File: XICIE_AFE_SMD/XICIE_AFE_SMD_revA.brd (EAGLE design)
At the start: 43.2 x 34 mm, 39 parts, among them IC1 LM324D, IC2 CY8C4245T, IC3 AAT1217, J1 22-27-2021-02, Q1 MOSFET-NCHANNELBSS123LT1G, Q2 MOSFET-NCHANNELBSS123LT1G, Q3 MOSFET-NCHANNELBSS123LT1G

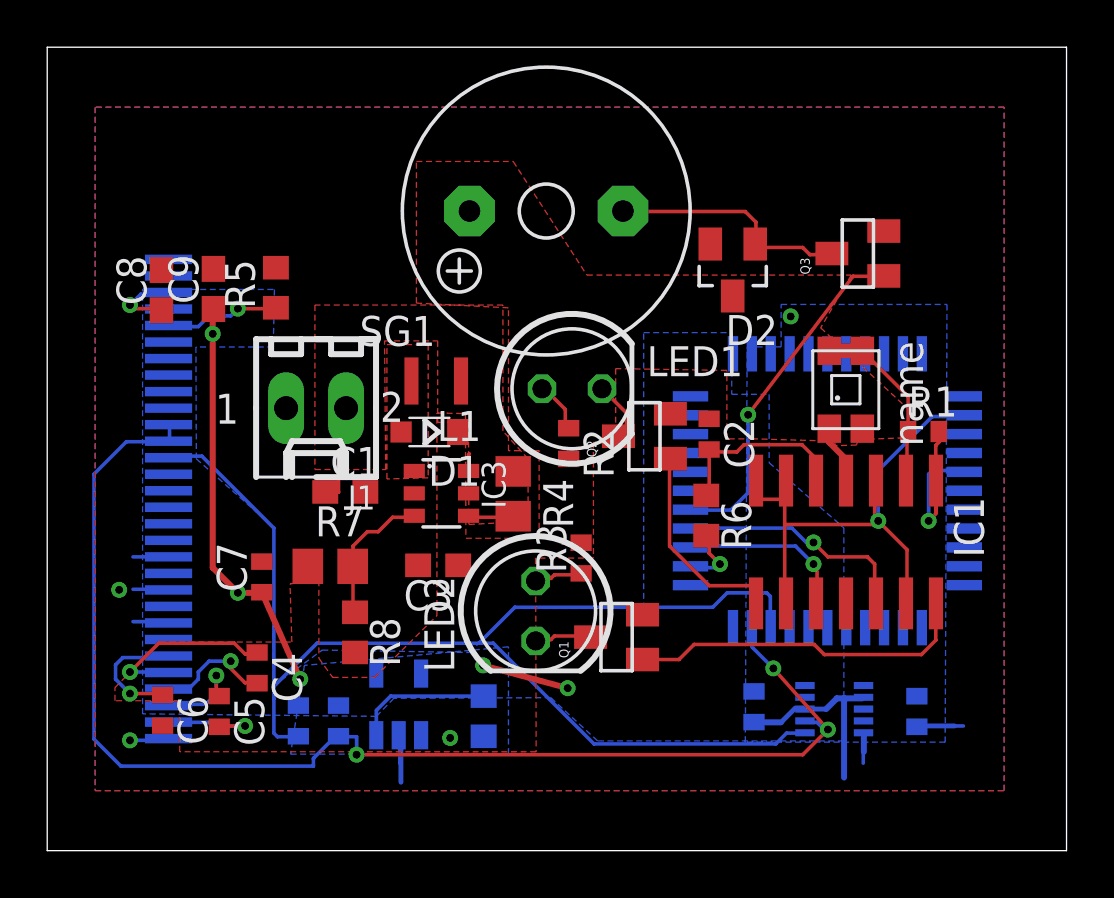
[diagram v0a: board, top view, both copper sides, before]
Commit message: Increased clearance for better manufacturing
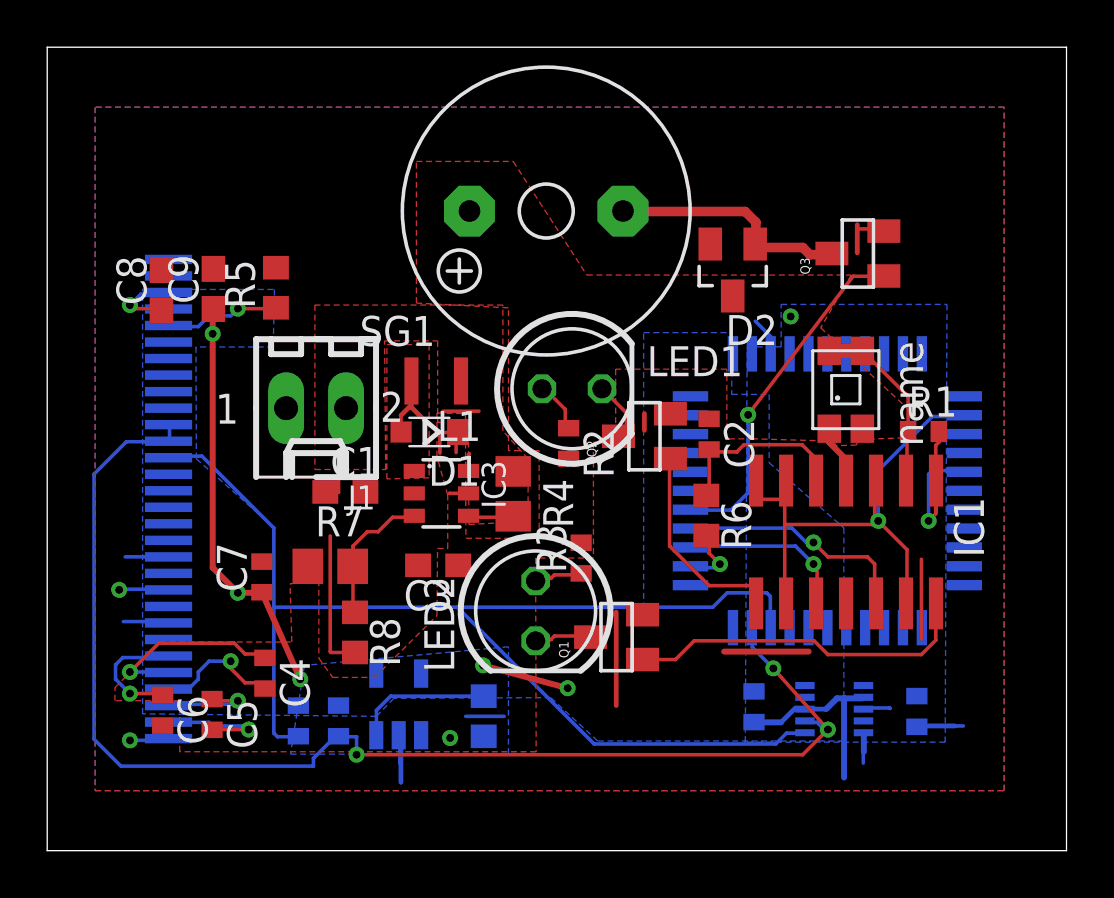
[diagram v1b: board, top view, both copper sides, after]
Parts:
- moved C4 0.40 mm to (32.1, 52.2)
- moved C5 0.33 mm to (29.8, 50.5)
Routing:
- net GND: track 23.6 -> 46.5 mm
- net +3V3: track 8.78 -> 14.8 mm
- net SW: track 0.00 -> 2.99 mm
- net VBAT: track 2.26 -> 3.79 mm
- net C2P: track 4.42 -> 5.29 mm
